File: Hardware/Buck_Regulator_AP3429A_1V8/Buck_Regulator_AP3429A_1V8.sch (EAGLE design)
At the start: 28 parts, among them J1 Screw Terminal, J2 POWER_JACKPOWER_JACK_SLOT_COM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, J3 Breakout Headers, U1 AP3429/A

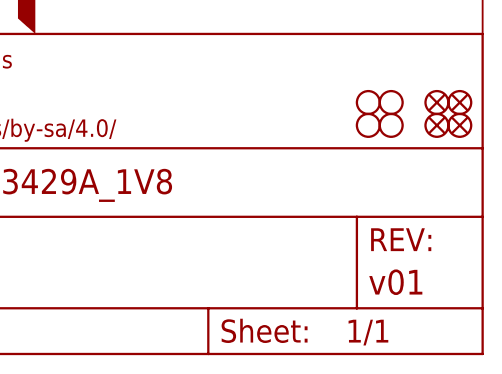
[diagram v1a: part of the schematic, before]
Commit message: Changed version number in schematic, adjusted components
Moved around some silkscreen in order for easier reading on the backside; changed the version number in the schematic to v10
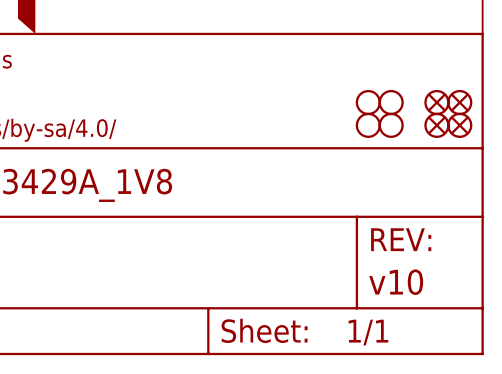
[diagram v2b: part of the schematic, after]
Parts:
- FRAME1: REV v01 -> v10
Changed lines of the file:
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@@
 <grid distance="0.1" unitdist="inch" unit="inch" style="lines" multiple="1" display="no" altdistance="0.01" altunitdist="inch" altunit="inch"/>
 <layers>
-<layer number="1" name="Top" color="4" fill="1" visible="yes" active="no"/>
-<layer number="2" name="Route2" color="16" fill="1" visible="yes" active="no"/>
-<layer number="15" name="Route15" color="23" fill="1" visible="yes" active="no"/>
-<layer number="16" name="Bottom" color="1" fill="1" visible="yes" active="no"/>
-<layer number="17" name="Pads" color="2" fill="1" visible="yes" active="no"/>
-<layer number="18" name="Vias" color="2" fill="1" visible="yes" active="no"/>
-<layer number="19" name="Unrouted" color="6" fill="1" visible="yes" active="no"/>
-<layer number="20" name="Dimension" color="24" fill="1" visible="yes" active="no"/>
-<layer number="21" name="tPlace" color="16" fill="1" visible="yes" active="no"/>
-<layer number="22" name="bPlace" color="14" fill="1" visible="yes" active="no"/>
-<layer number="23" name="tOrigins" color="15" fill="1" visible="yes" active="no"/>
-<layer number="24" name="bOrigins" color="15" fill="1" visible="yes" active="no"/>
-<layer number="25" name="tNames" color="7" fill="1" visible="yes" active="no"/>
-<layer number="26" name="bNames" color="7" fill="1" visible="yes" active="no"/>
-<layer number="27" name="tValues" color="7" fill="1" visible="yes" active="no"/>
-<layer number="28" name="bValues" color="7" fill="1" visible="yes" active="no"/>
+<layer number="1" name="Top" color="4" fill="1" visible="no" active="no"/>
+<layer number="2" name="Route2" color="16" fill="1" visible="no" active="no"/>
+<layer number="15" name="Route15" color="23" fill="1" visible="no" active="no"/>
+<layer number="16" name="Bottom" color="1" fill="1" visible="no" active="no"/>
+<layer number="17" name="Pads" color="2" fill="1" visible="no" active="no"/>
+<layer number="18" name="Vias" color="2" fill="1" visible="no" active="no"/>
+<layer number="19" name="Unrouted" color="6" fill="1" visible="no" active="no"/>
+<layer number="20" name="Dimension" color="24" fill="1" visible="no" active="no"/>
+<layer number="21" name="tPlace" color="16" fill="1" visible="no" active="no"/>
+<layer number="22" name="bPlace" color="14" fill="1" visible="no" active="no"/>
+<layer number="23" name="tOrigins" color="15" fill="1" visible="no" active="no"/>
+<layer number="24" name="bOrigins" color="15" fill="1" visible="no" active="no"/>
+<layer number="25" name="tNames" color="7" fill="1" visible="no" active="no"/>
+<layer number="26" name="bNames" color="7" fill="1" visible="no" active="no"/>
+<layer number="27" name="tValues" color="7" fill="1" visible="no" active="no"/>
+<layer number="28" name="bValues" color="7" fill="1" visible="no" active="no"/>
 <layer number="29" name="tStop" color="7" fill="3" visible="no" active="no"/>
 <layer number="30" name="bStop" color="7" fill="6" visible="no" active="no"/>
@@
 <layer number="35" name="tGlue" color="7" fill="4" visible="no" active="no"/>
 <layer number="36" name="bGlue" color="7" fill="5" visible="no" active="no"/>
-<layer number="37" name="tTest" color="7" fill="1" visible="yes" active="no"/>
-<layer number="38" name="bTest" color="7" fill="1" visible="yes" active="no"/>
+<layer number="37" name="tTest" color="7" fill="1" visible="no" active="no"/>
+<layer number="38" name="bTest" color="7" fill="1" visible="no" active="no"/>
 <layer number="39" name="tKeepout" color="4" fill="11" visible="no" active="no"/>
 <layer number="40" name="bKeepout" color="1" fill="11" visible="no" active="no"/>
@@
 <layer number="44" name="Drills" color="7" fill="1" visible="no" active="no"/>
 <layer number="45" name="Holes" color="7" fill="1" visible="no" active="no"/>
-<layer number="46" name="Milling" color="3" fill="1" visible="yes" active="no"/>
-<layer number="47" name="Measures" color="7" fill="1" visible="yes" active="no"/>
-<layer number="48" name="Document" color="7" fill="1" visible="yes" active="no"/>
-<layer number="49" name="Reference" color="7" fill="1" visible="yes" active="no"/>
-<layer number="50" name="dxf" color="7" fill="1" visible="yes" active="no"/>
-<layer number="51" name="tDocu" color="6" fill="1" visible="yes" active="no"/>
-<layer number="52" name="bDocu" color="7" fill="1" visible="yes" active="no"/>
-<layer number="53" name="tGND_GNDA" color="7" fill="9" visible="yes" active="no"/>
-<layer number="54" name="bGND_GNDA" color="1" fill="9" visible="yes" active="no"/>
-<layer number="56" name="wert" color="7" fill="1" visible="yes" active="no"/>
-<layer number="57" name="tCAD" color="7" fill="1" visible="yes" active="no"/>
-<layer number="58" name="bCAD" color="7" fill="1" visible="yes" active="no"/>
-<layer number="59" name="tCarbon" color="7" fill="1" visible="yes" active="no"/>
-<layer number="60" name="bCarbon" color="7" fill="1" visible="yes" active="no"/>
+<layer number="46" name="Milling" color="3" fill="1" visible="no" active="no"/>
+<layer number="47" name="Measures" color="7" fill="1" visible="no" active="no"/>
+<layer number="48" name="Document" color="7" fill="1" visible="no" active="no"/>
+<layer number="49" name="Reference" color="7" fill="1" visible="no" active="no"/>
+<layer number="50" name="dxf" color="7" fill="1" visible="no" active="no"/>
+<layer number="51" name="tDocu" color="6" fill="1" visible="no" active="no"/>
+<layer number="52" name="bDocu" color="7" fill="1" visible="no" active="no"/>
+<layer number="53" name="tGND_GNDA" color="7" fill="9" visible="no" active="no"/>
+<layer number="54" name="bGND_GNDA" color="1" fill="9" visible="no" active="no"/>
+<layer number="56" name="wert" color="7" fill="1" visible="no" active="no"/>
+<layer number="57" name="tCAD" color="7" fill="1" visible="no" active="no"/>
+<layer number="58" name="bCAD" color="7" fill="1" visible="no" active="no"/>
+<layer number="59" name="tCarbon" color="7" fill="1" visible="no" active="no"/>
+<layer number="60" name="bCarbon" color="7" fill="1" visible="no" active="no"/>
 <layer number="88" name="SimResults" color="9" fill="1" visible="yes" active="yes"/>
 <layer number="89" name="SimProbes" color="9" fill="1" visible="yes" active="yes"/>
@@
 <part name="FRAME1" library="SparkFun-Aesthetics" deviceset="FRAME-LEDGER" device="">
 <attribute name="DESIGNER" value="M. Chodikov"/>
-<attribute name="REV" value="v01"/>
+<attribute name="REV" value="v10"/>
 </part>
 <part name="FD1" library="SparkFun-Aesthetics" deviceset="FIDUCIAL" device="UFIDUCIAL"/>

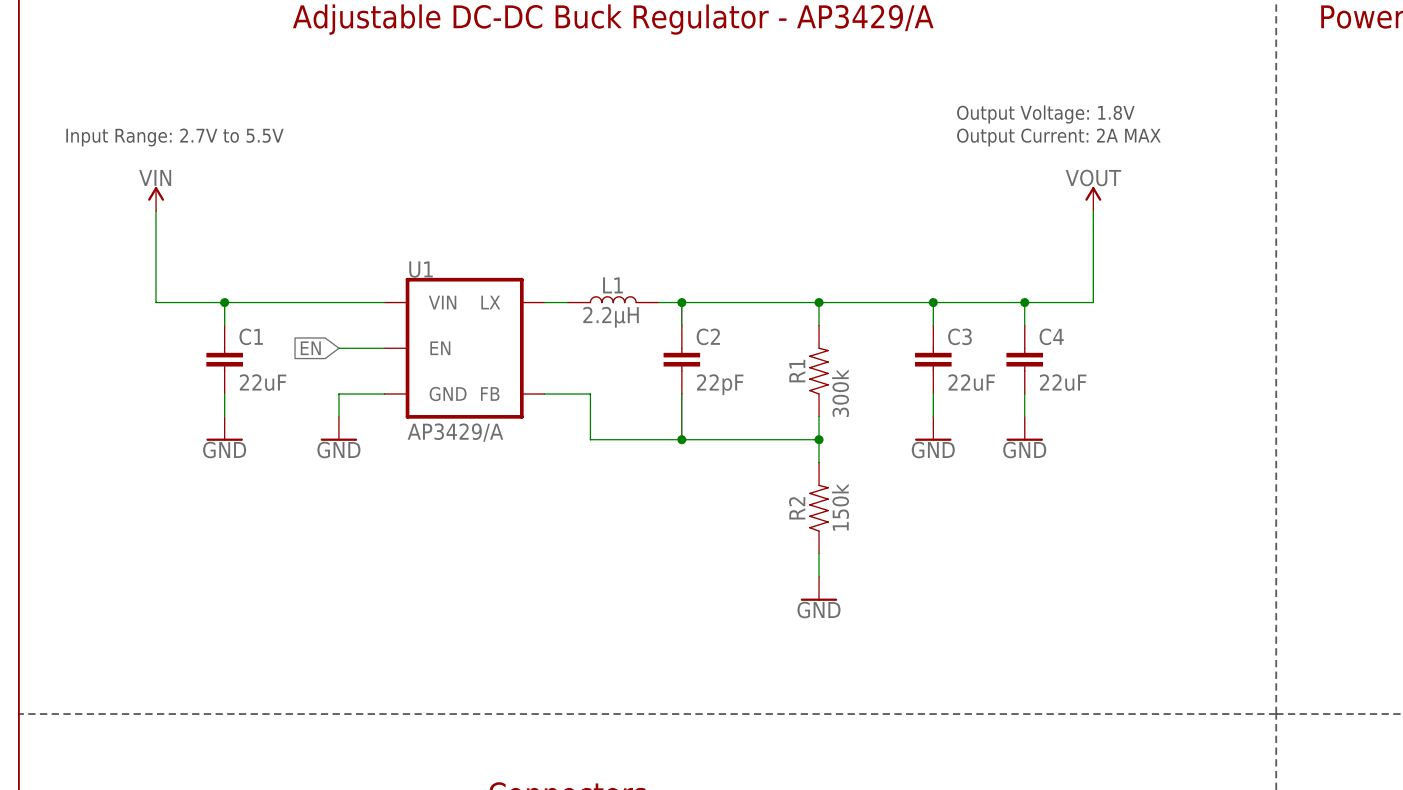
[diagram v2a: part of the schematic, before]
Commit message: Added 2 more output capacitors
Added more output capacitance to match ALC block - there was some ripple detected during testing so adding these should eliminate that. Adjusted the components on the board accordingly then matched the exact locations of said movement for each board.
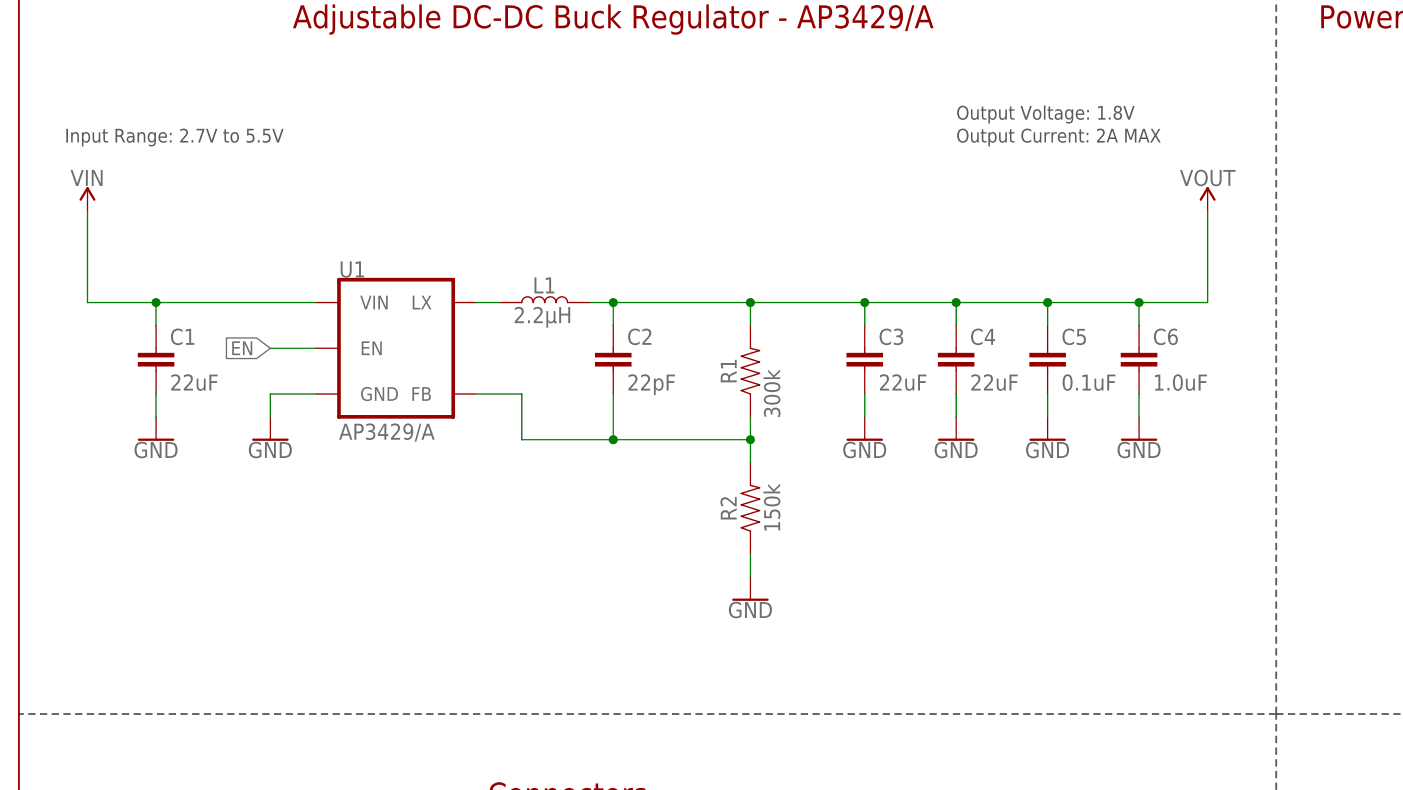
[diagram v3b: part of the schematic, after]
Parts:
- added C5: 0.1uF, SparkFun-Capacitors:0.1UF-0603-25V-5%
- added C6: 1.0uF, SparkFun-Capacitors:1.0UF-0603-16V-10%-X7R
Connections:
- net GND: now also C5.2, C6.2
- net VOUT: now also C5.1, C6.1
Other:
- moved on the sheet: C1, C2, C3, C4, L1, R1, R2, U1

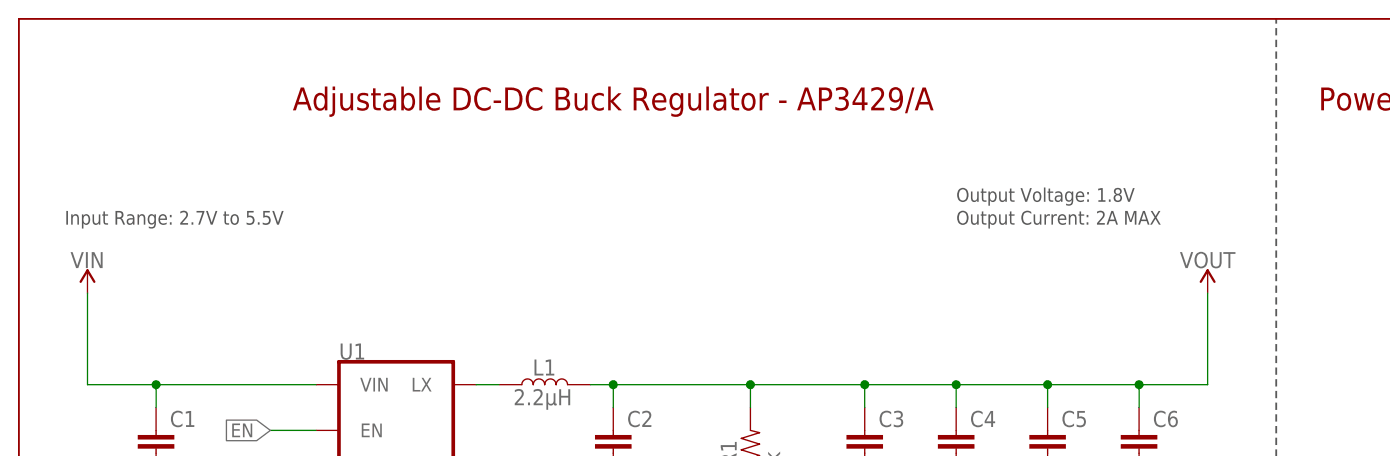
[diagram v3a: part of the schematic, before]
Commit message: Design Review changes
Cleaned up 1.8V Hardware folder by deleting unneeded files, adjusted schematic notes for easier reading, deleted extraneous measures, adjusted GND via sizes to be the same size (15mil), adjusted some vias for better GND plane connection
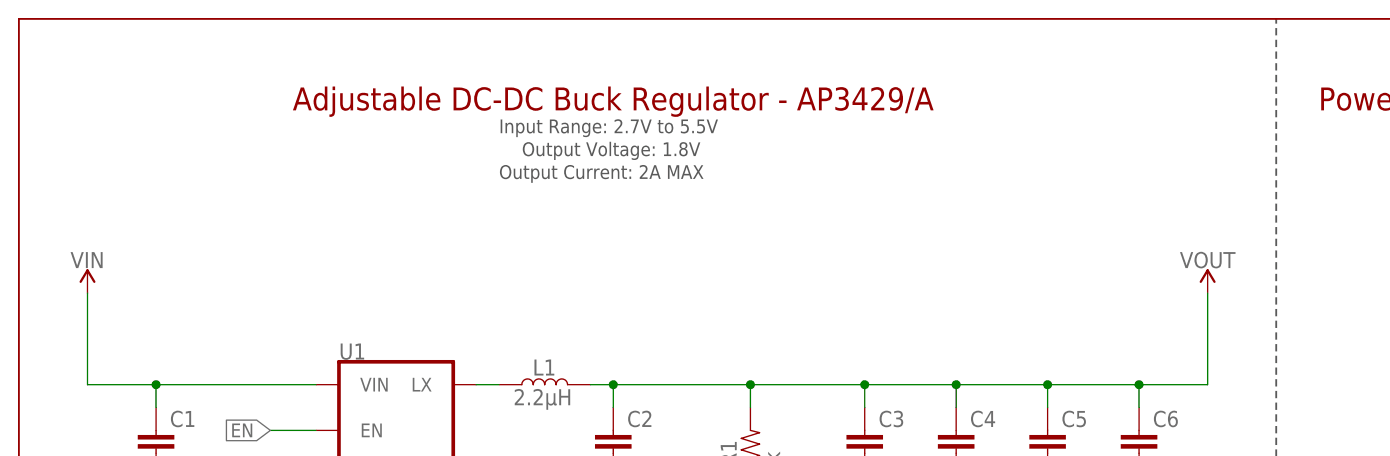
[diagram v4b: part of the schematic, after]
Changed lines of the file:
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@@
 <sheet>
 <plain>
-<text x="5.08" y="127" size="1.524" layer="97" font="vector">Input Range: 2.7V to 5.5V</text>
+<text x="53.34" y="137.16" size="1.524" layer="97" font="vector">Input Range: 2.7V to 5.5V</text>
 <wire x1="0" y1="0" x2="139.7" y2="0" width="0.2032" layer="94"/>
 <wire x1="241.3" y1="35.56" x2="241.3" y2="149.86" width="0.2032" layer="94"/>
@@
 <wire x1="139.7" y1="63.5" x2="0" y2="63.5" width="0.2032" layer="97" style="longdash"/>
 <text x="58.42" y="37.084" size="1.524" layer="97" font="vector">POWER_JACK</text>
-<text x="104.14" y="127" size="1.524" layer="97" font="vector">Output Current: 2A MAX</text>
+<text x="53.34" y="132.08" size="1.524" layer="97" font="vector">Output Current: 2A MAX</text>
 <text x="45.72" y="5.08" size="1.524" layer="97" font="vector">WARNING: Only connect one Vin input at a time</text>
 <wire x1="139.7" y1="63.5" x2="139.7" y2="149.86" width="0.2032" layer="97" style="longdash"/>
@@
 to disconnect
 LED.</text>
-<text x="104.14" y="129.54" size="1.524" layer="97" font="vector">Output Voltage: 1.8V</text>
+<text x="55.88" y="134.62" size="1.524" layer="97" font="vector">Output Voltage: 1.8V</text>
 </plain>
 <instances>
